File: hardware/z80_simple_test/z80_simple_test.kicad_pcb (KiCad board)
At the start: 2 copper layers, 95 x 100 mm, 51 parts, among them J1 Barrel_Jack_Switch, J2 Conn_02x15_Odd_Even, U1 Z84C000XPEG, U2 SRAM_512K8B_DIP_SOP_SOJ, U3 EEPROM_512K8B_DIP, U4 74XX138, U5 Z84C40XPEG, U6 74XX32, U7 74XX00

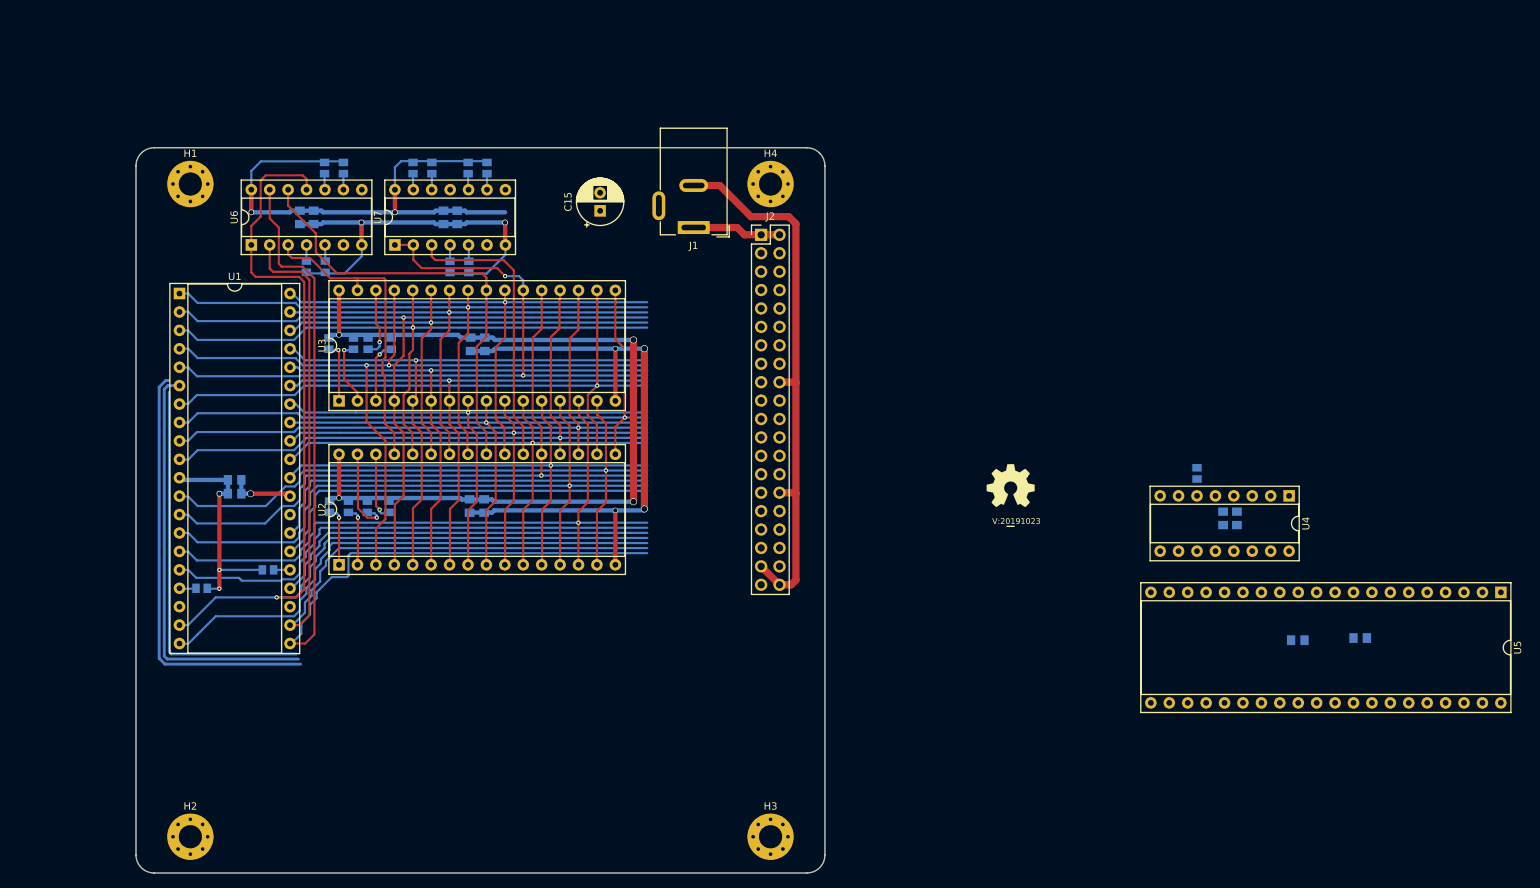
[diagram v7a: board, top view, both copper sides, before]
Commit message: started placement of SIO
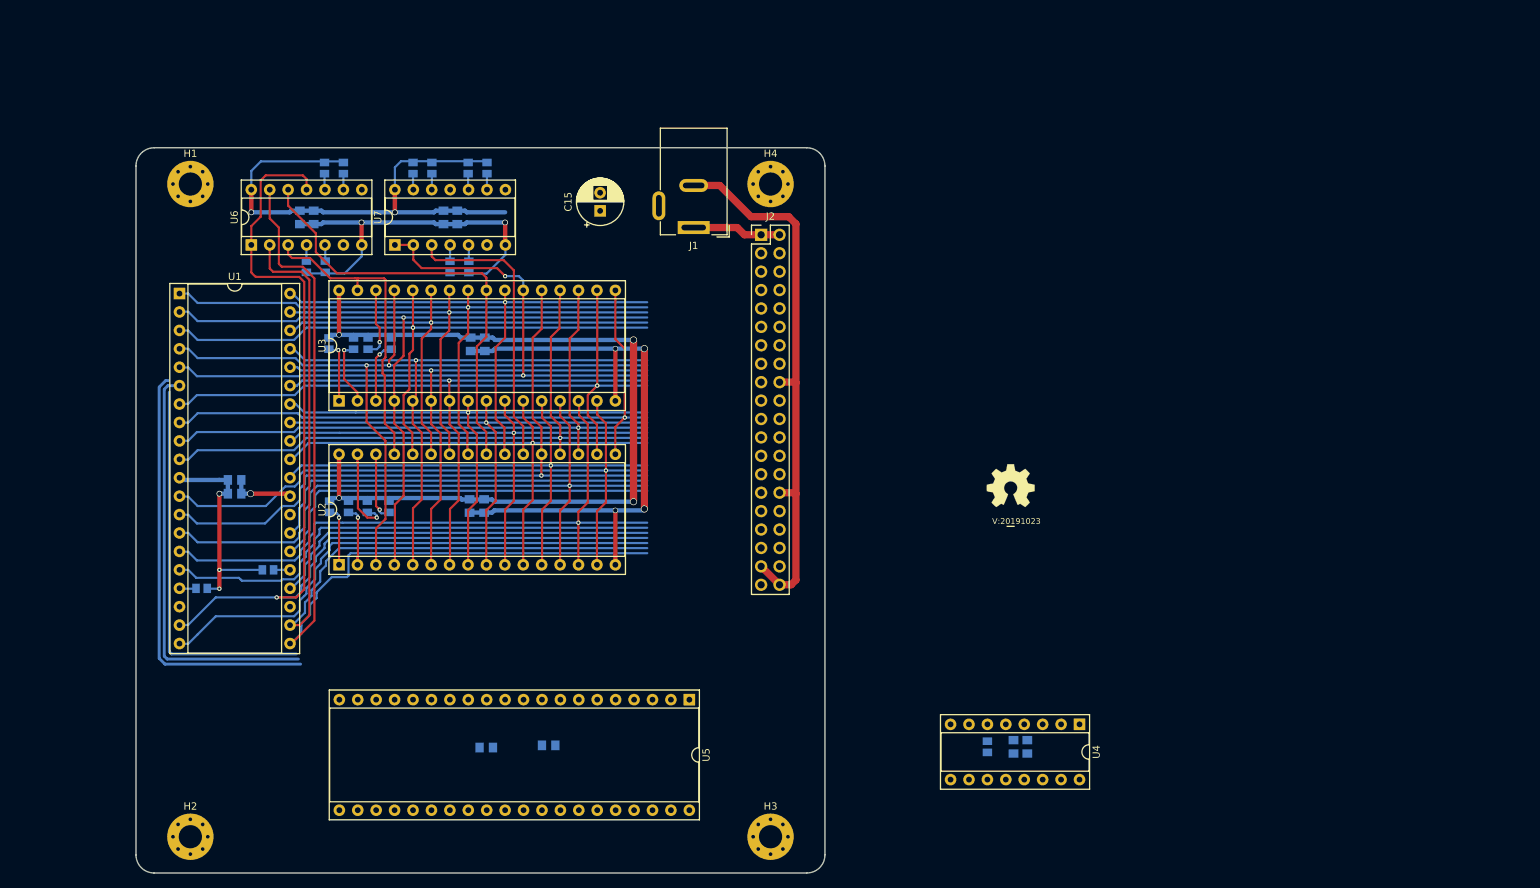
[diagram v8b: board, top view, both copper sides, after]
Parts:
- moved C10 112.9 mm to (159.4, 132.4)
- moved C9 112.9 mm to (150.8, 132.7)
- moved U5 112.9 mm to (178.8, 126.1)
- moved R2 47.5 mm to (219.9, 132.6), turned to 270 degrees
- moved C7 42.7 mm to (223.5, 132.6)
- moved C8 42.7 mm to (225.4, 132.6)
- moved U4 42.7 mm to (232.6, 129.5)
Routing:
- net /!RD: track 127.9 -> 126.8 mm
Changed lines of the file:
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@@
   )
   (setup
-    (last_trace_width 0.3)
+    (last_trace_width 0.4)
     (user_trace_width 0.15)
     (user_trace_width 0.2)
@@
   )
   (module SquantorRcl:R_0805+0603 (layer B.Cu)
-    (at 248.8 94.9 90)
+    (at 219.9 132.6 270)
     (descr "Resistor SMD 0805, reflow soldering, Vishay (see dcrcw.pdf)")
     (tags "resistor 0805")
@@
     (fp_line (start 1 -0.625) (end -1 -0.625) (layer B.Fab) (width 0.1))
     (fp_line (start -1 -0.625) (end -1 0.625) (layer B.Fab) (width 0.1))
-    (pad 2 smd rect (at 0.775 0 90) (size 1.05 1.3) (layers B.Cu B.Paste B.Mask)
+    (pad 2 smd rect (at 0.775 0 270) (size 1.05 1.3) (layers B.Cu B.Paste B.Mask)
       (net 2 /VDD))
-    (pad 1 smd rect (at -0.775 0 90) (size 1.05 1.3) (layers B.Cu B.Paste B.Mask)
+    (pad 1 smd rect (at -0.775 0 270) (size 1.05 1.3) (layers B.Cu B.Paste B.Mask)
       (net 38 "Net-(R2-Pad1)"))
     (model ${KISYS3DMOD}/Resistor_SMD.3dshapes/R_0805_2012Metric.step
@@
   )
   (module Package_DIP:DIP-40_W15.24mm_Socket (layer F.Cu)
-    (at 290.7 111.3 270)
+    (at 178.8 126.1 270)
     (descr "40-lead though-hole mounted DIP package, row spacing 15.24 mm (600 mils), Socket")
     (tags "THT DIP DIL PDIP 2.54mm 15.24mm 600mil Socket")
@@
   )
   (module SquantorRcl:C_0805+0603 (layer B.Cu)
-    (at 271.3 117.6)
+    (at 159.4 132.4)
     (descr "Capacitor SMD 0805 and 0603 pad sizes, reflow soldering, based on AVX dimensions")
     (tags "capacitor 0805 0603 mixed")
@@
   )
   (module SquantorRcl:C_0805+0603 (layer B.Cu)
-    (at 262.7 117.9)
+    (at 150.8 132.7)
     (descr "Capacitor SMD 0805 and 0603 pad sizes, reflow soldering, based on AVX dimensions")
     (tags "capacitor 0805 0603 mixed")
@@
   )
   (module Package_DIP:DIP-16_W7.62mm_Socket (layer F.Cu)
-    (at 261.5 98 270)
+    (at 232.6 129.5 270)
     (descr "16-lead though-hole mounted DIP package, row spacing 7.62 mm (300 mils), Socket")
     (tags "THT DIP DIL PDIP 2.54mm 7.62mm 300mil Socket")
@@
   )
   (module SquantorRcl:C_0805+0603 (layer B.Cu)
-    (at 254.3 101.1 270)
+    (at 225.4 132.6 270)
     (descr "Capacitor SMD 0805 and 0603 pad sizes, reflow soldering, based on AVX dimensions")
     (tags "capacitor 0805 0603 mixed")
@@
   )
   (module SquantorRcl:C_0805+0603 (layer B.Cu)
-    (at 252.4 101.1 270)
+    (at 223.5 132.6 270)
     (descr "Capacitor SMD 0805 and 0603 pad sizes, reflow soldering, based on AVX dimensions")
     (tags "capacitor 0805 0603 mixed")
@@
   (segment (start 122.2 61) (end 120.94 59.74) (width 0.3) (layer F.Cu) (net 33))
   (segment (start 122.2 66) (end 122.2 61) (width 0.3) (layer F.Cu) (net 33))
-  (segment (start 125.84 118.36) (end 127.1 117.1) (width 0.3) (layer F.Cu) (net 33))
-  (segment (start 123.74 118.36) (end 125.84 118.36) (width 0.3) (layer F.Cu) (net 33))
-  (segment (start 127.1 117.1) (end 127.1 68) (width 0.3) (layer F.Cu) (net 33))
+  (segment (start 123.94 118.36) (end 127.1 115.2) (width 0.3) (layer F.Cu) (net 33))
+  (segment (start 123.74 118.36) (end 123.94 118.36) (width 0.3) (layer F.Cu) (net 33))
   (segment (start 127.1 68) (end 125.5 66.4) (width 0.3) (layer F.Cu) (net 33))
+  (segment (start 127.1 115.2) (end 127.1 68) (width 0.3) (layer F.Cu) (net 33))
   (segment (start 125.5 66.4) (end 122.6 66.4) (width 0.3) (layer F.Cu) (net 33))
   (segment (start 122.6 66.4) (end 122.2 66) (width 0.3) (layer F.Cu) (net 33))
